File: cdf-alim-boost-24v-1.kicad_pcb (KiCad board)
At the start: 4 copper layers, 70 x 50 mm, 99 parts, among them J1 Conn_01x02, J2 Conn_01x02, J3 Conn_01x02, Q1 BSC019N04LS, Q2 BSC019N04LS, Q3 BSC019N04LS, Q4 BSC019N04LS, Q5 BSC019N04LS, U1 HT753-1, U2 TPS25983, U4 LM5122

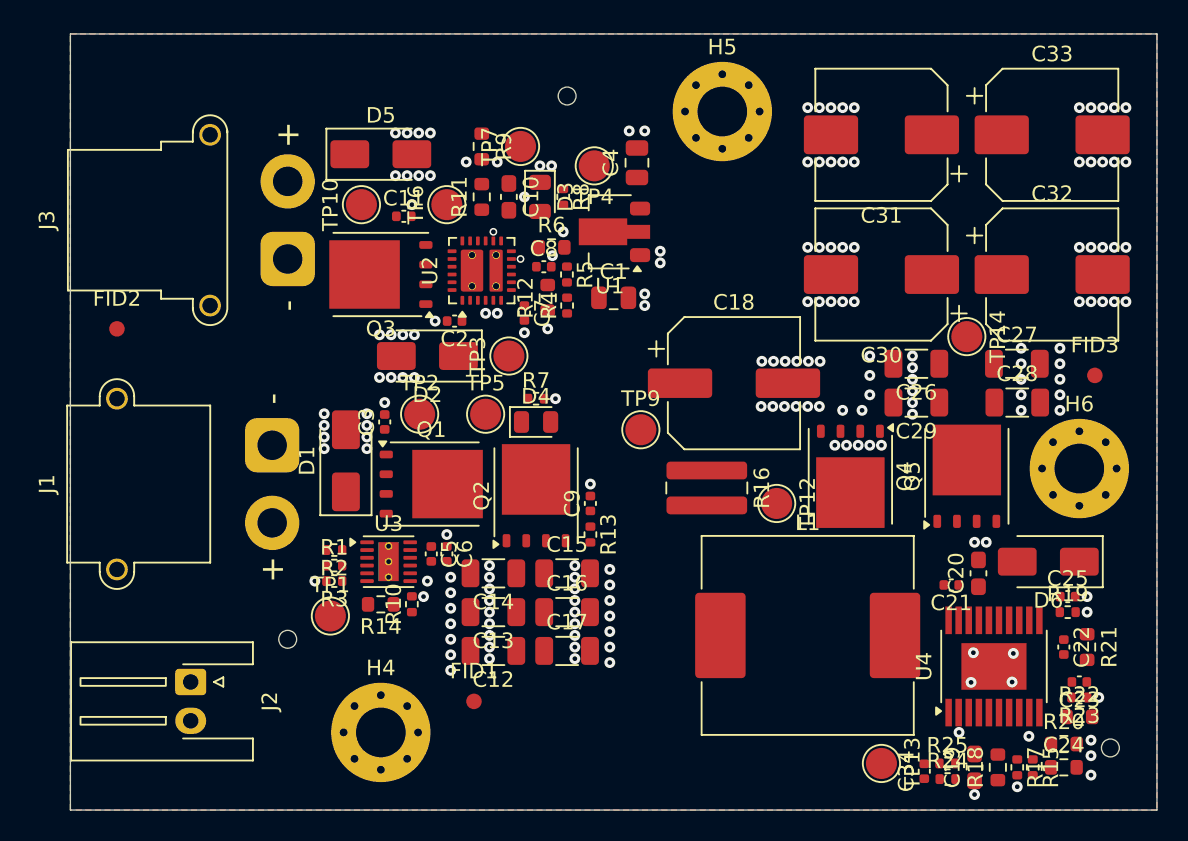
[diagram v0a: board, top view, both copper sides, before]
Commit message: pcb: add main power path routing
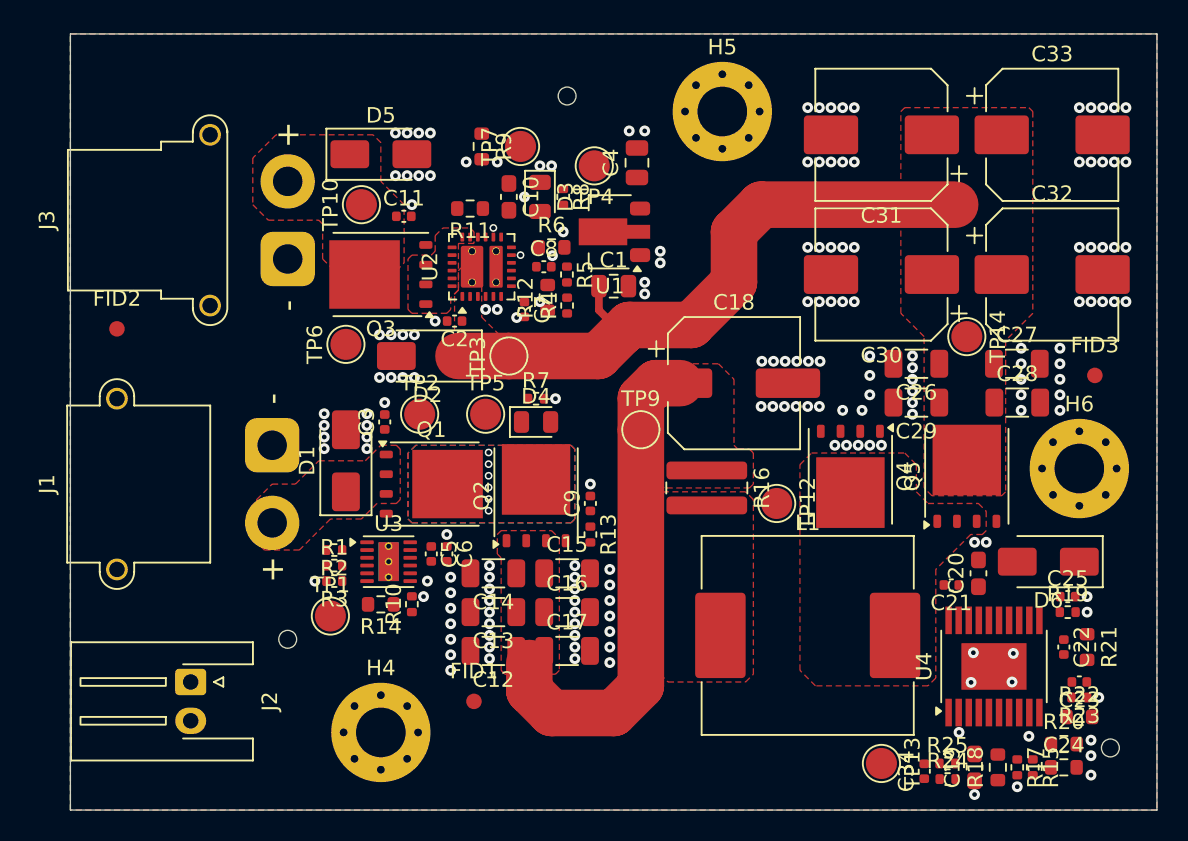
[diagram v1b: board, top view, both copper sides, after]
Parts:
- moved TP6 11.1 mm to (132.8, 88.0)
- moved R11 1.06 mm to (140.8, 79.2), turned to 180 degrees
- moved C1 0.75 mm to (150.0, 84.2)
- moved U2 0.25 mm to (141.5, 83.0)
- moved C7 0.23 mm to (144.2, 85.8)
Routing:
- net +24V: track 0.00 -> 41.5 mm
- net +18V: track 0.14 -> 31.9 mm
- net Net-(D4-A): vias 0 -> 6
- added copper zone on F.Cu, net +18V
- added copper zone on F.Cu, net +24V
- added copper zone on F.Cu, net +BATT
- added copper zone on B.Cu, net Net-(D4-A)
- added copper zone on F.Cu, net Net-(D4-A)
- added copper zone on F.Cu, net Net-(D5-K)
- added copper zone on F.Cu, net Net-(L1-Pad1)
- added copper zone on F.Cu, net Net-(Q3-S-Pad1)
- added copper zone on F.Cu, net Net-(Q4-D)

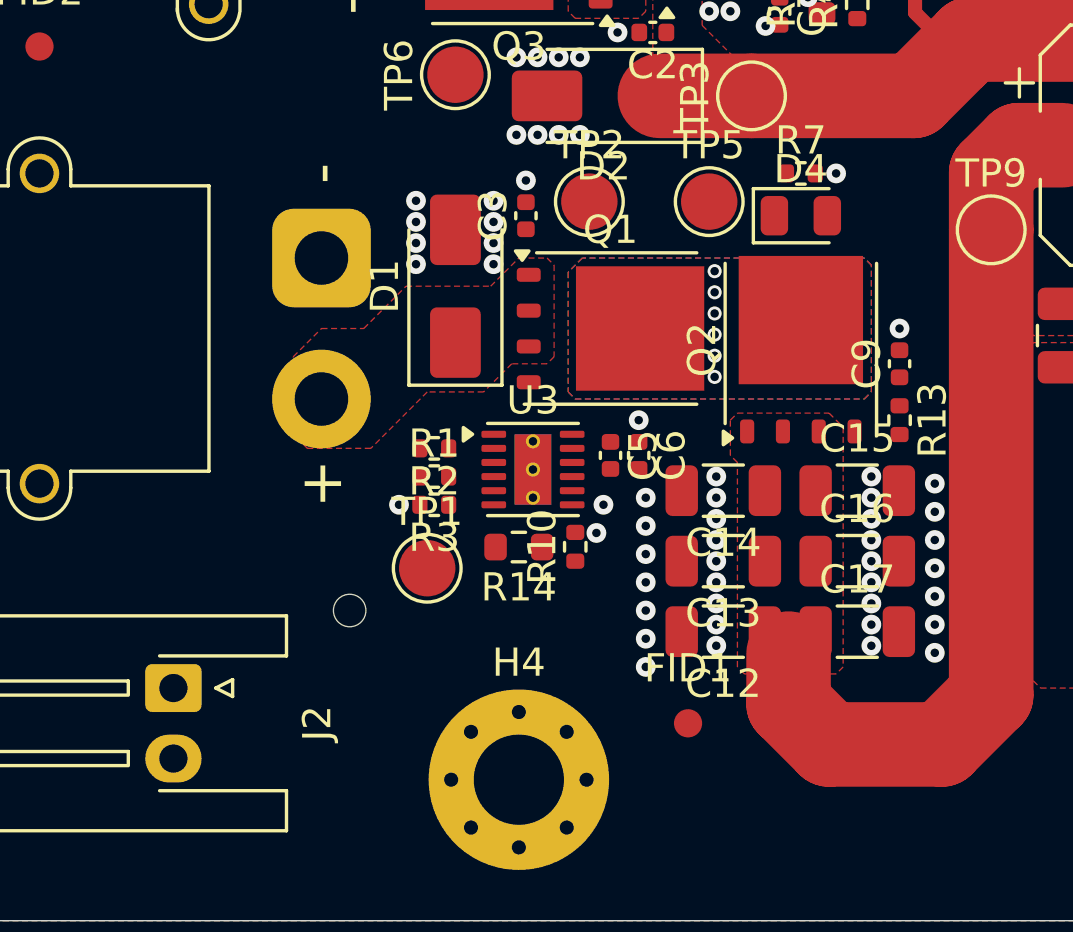
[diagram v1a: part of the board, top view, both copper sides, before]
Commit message: pcb: add efuse routing
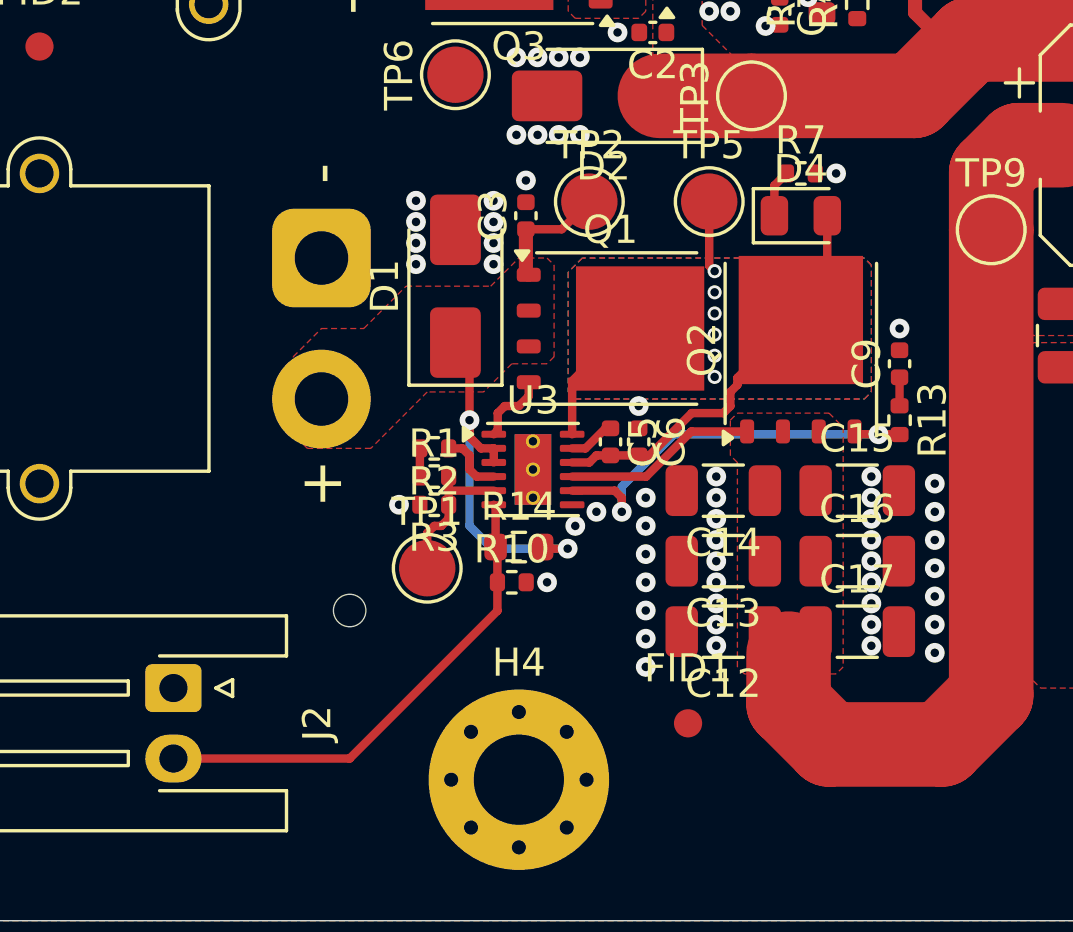
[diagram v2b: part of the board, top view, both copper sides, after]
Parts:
- moved R10 2.58 mm to (134.8, 106.0), turned to 0 degrees
- moved C5 0.48 mm to (138.2, 101.0)
- moved C6 0.48 mm to (139.2, 101.0)
- turned R14 to 0 degrees
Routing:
- net Net-(D4-A): track 0.00 -> 23.9 mm
- net +BATT: track 0.00 -> 17.9 mm, vias 0 -> 2
- net Net-(J2-B): track 0.00 -> 17.5 mm
- net Net-(Q2-G): track 0.00 -> 14.8 mm, vias 0 -> 2
- net +18V: track 31.9 -> 38.8 mm
- net Net-(U3-OV): track 0.00 -> 5.31 mm
- net Net-(Q1-G): track 0.00 -> 2.65 mm
- net Net-(U3-SW): track 0.00 -> 2.31 mm
- net Net-(D4-K): track 0.00 -> 1.68 mm
- net Net-(U3-CAP): track 0.00 -> 1.65 mm
- net Net-(C9-Pad1): track 0.00 -> 1.01 mm
- net /VBATT: track 0.00 -> 1.00 mm
- net GND: vias 178 -> 179

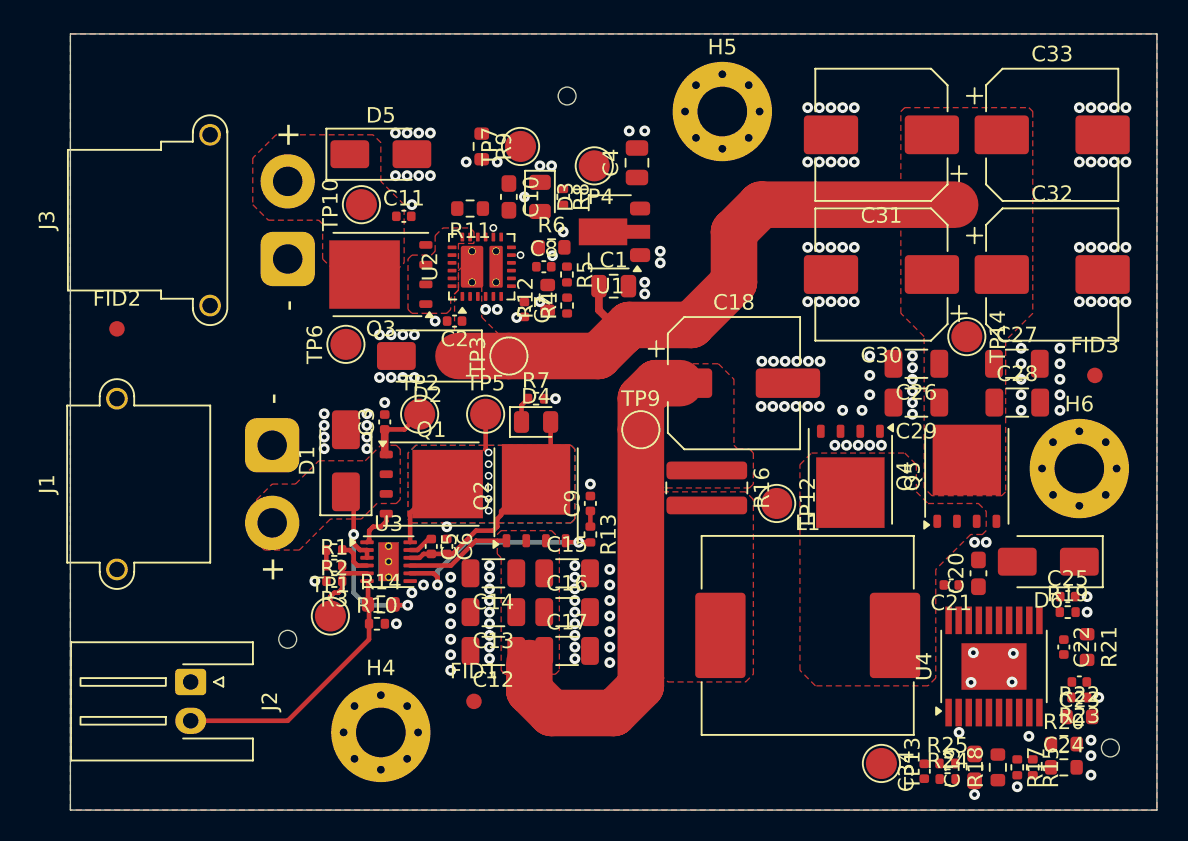
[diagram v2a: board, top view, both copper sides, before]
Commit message: pcb: add smps routing
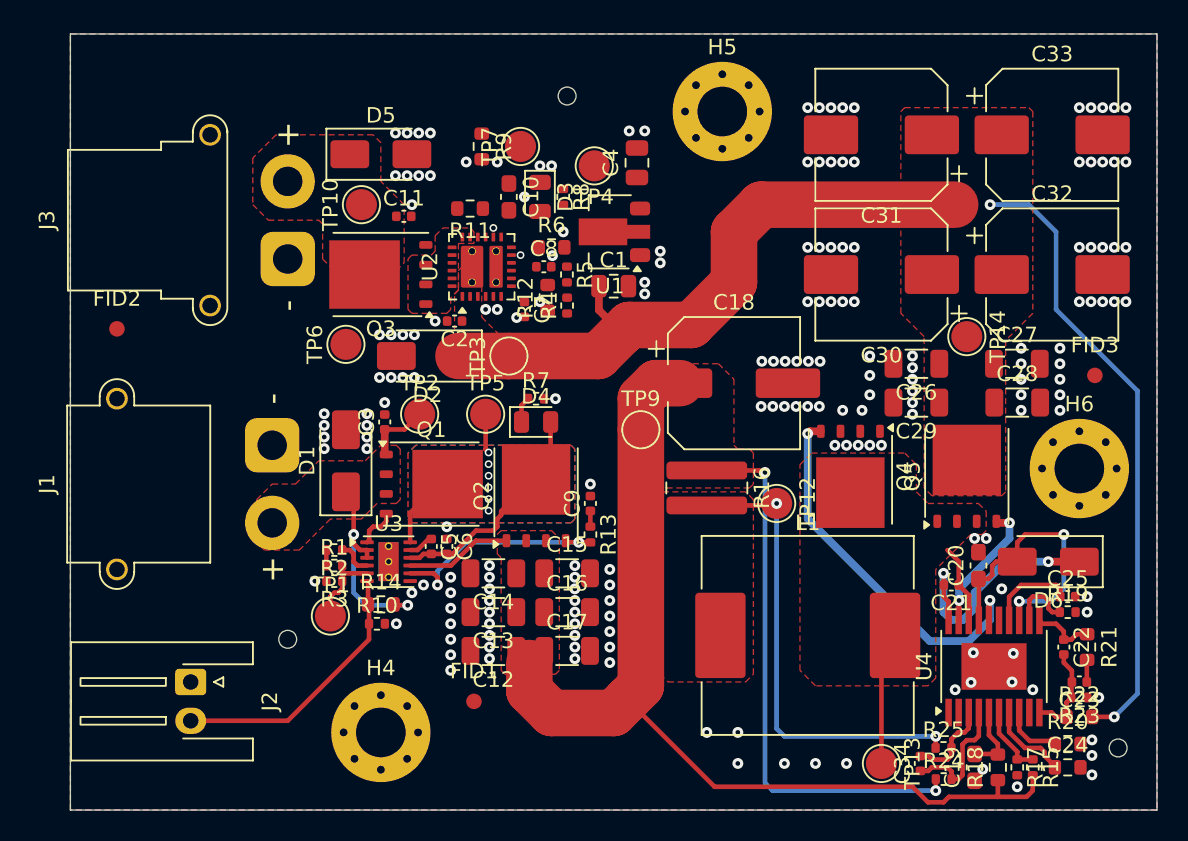
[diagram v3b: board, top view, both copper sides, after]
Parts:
- moved R25 1.03 mm to (171.2, 114.0)
- moved C34 0.56 mm to (169.8, 115.0)
- moved C20 0.50 mm to (173.5, 102.2)
- moved H2 0.50 mm to (182.5, 114.0)
- moved C24 0.25 mm to (179.2, 115.2)
- moved R20 0.25 mm to (179.2, 113.8)
- moved R24 0.25 mm to (171.3, 116.0)
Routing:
- net +18V: track 38.8 -> 105.8 mm, vias 0 -> 2
- net +24V: track 41.5 -> 82.0 mm, vias 0 -> 2
- net Net-(L1-Pad1): track 0.00 -> 30.4 mm, vias 0 -> 2
- net Net-(Q4-G): track 0.00 -> 24.6 mm, vias 0 -> 2
- net +VCC: track 0.00 -> 18.4 mm, vias 0 -> 2
- net Net-(D6-K): track 0.00 -> 16.8 mm, vias 0 -> 2
- net Net-(Q4-D): track 0.00 -> 13.7 mm
- net Net-(Q5-G): track 0.00 -> 8.52 mm, vias 0 -> 2
- net Net-(U4-CSP): track 0.00 -> 8.27 mm
- net Net-(U4-FB): track 0.00 -> 6.24 mm
- net Net-(U4-RES): track 0.00 -> 5.71 mm
- net Net-(U4-CSN): track 0.00 -> 5.69 mm
- net Net-(U4-SS): track 0.00 -> 5.34 mm
- net Net-(U4-UVLO): track 0.00 -> 4.51 mm
- net Net-(U4-VIN): track 0.00 -> 4.46 mm
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
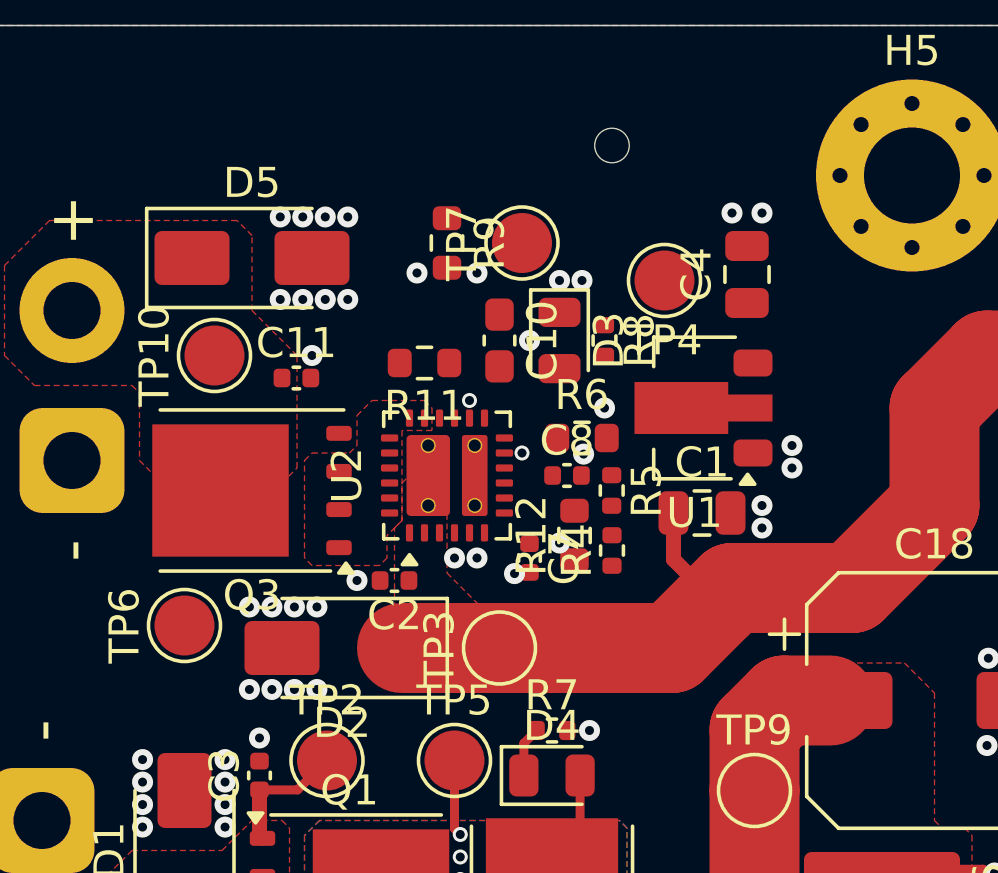
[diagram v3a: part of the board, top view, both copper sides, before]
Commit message: pcb: add efuse routing
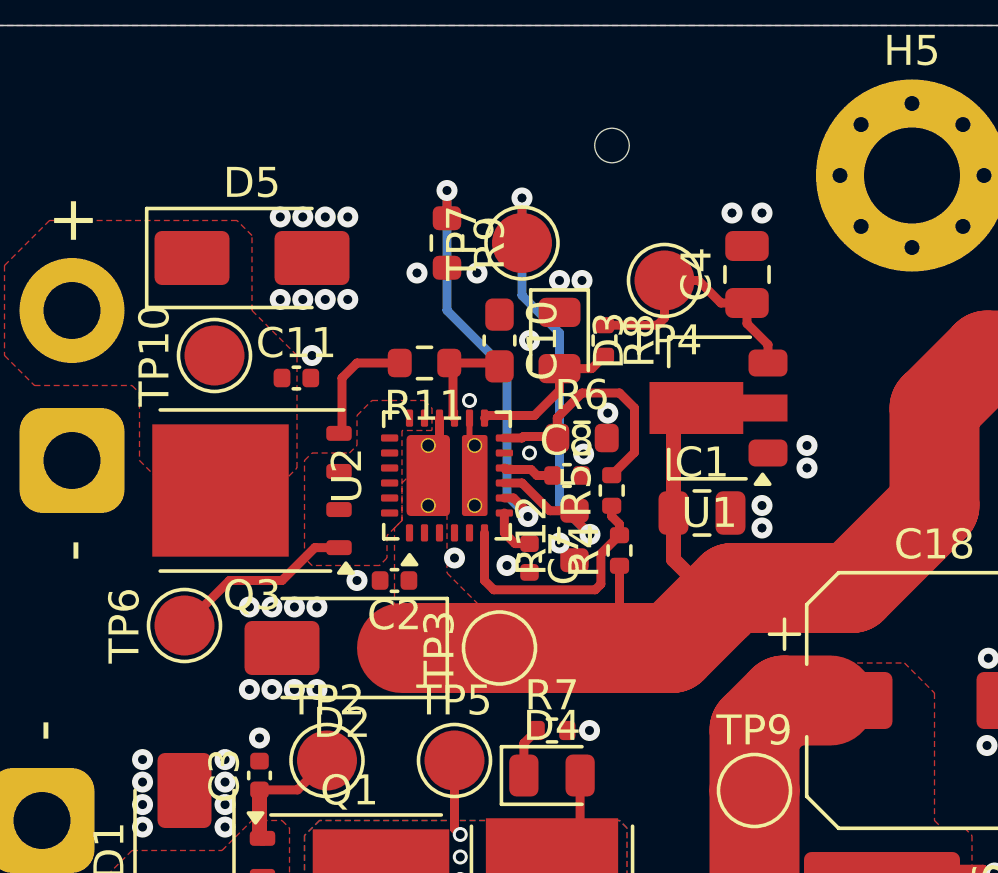
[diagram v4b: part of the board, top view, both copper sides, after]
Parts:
- moved U1 0.50 mm to (150.2, 80.8)
- moved R4 0.25 mm to (147.2, 85.5)
- turned R5 to 90 degrees
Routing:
- net Net-(U2-IMON): track 0.00 -> 17.4 mm, vias 0 -> 2
- net Net-(U2-ILIM): track 0.00 -> 14.0 mm, vias 0 -> 2
- net +24V: track 82.0 -> 93.1 mm
- net +3V3: track 0.00 -> 8.70 mm
- net Net-(U2-EN/UVLO): track 0.00 -> 8.65 mm
- net Net-(U2-OVLO): track 0.00 -> 8.16 mm
- net Net-(Q3-S-Pad1): track 0.00 -> 6.22 mm
- net Net-(D3-A): track 0.00 -> 5.29 mm
- net Net-(Q3-G): track 0.00 -> 4.02 mm
- net Net-(U2-dVdt/BGATE): track 0.00 -> 3.63 mm
- net Net-(U2-RETRY_DLY): track 0.00 -> 1.71 mm
- net Net-(U2-ITIMER): track 0.00 -> 1.65 mm
- net GND: track 0.00 -> 0.98 mm, vias 186 -> 185

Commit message: pcb: add stiching vias
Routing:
- net GND: vias 185 -> 265
